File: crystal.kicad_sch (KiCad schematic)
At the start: 3 parts, among them X2 25000000

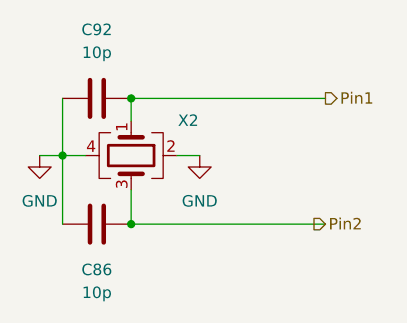
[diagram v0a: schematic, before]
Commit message: adds crystal for STM. Refs: #1
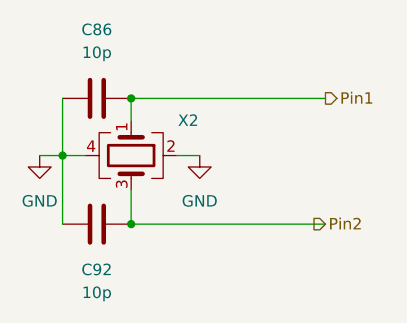
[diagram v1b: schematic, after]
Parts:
- renumbered C92 to C86, C86 to C92
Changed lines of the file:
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@@
 		(instances
 			(project "shish-lan"
-				(path "/d4536448-b109-4159-96e2-3dc21baf2d6e/06488c82-a47f-4277-b0ee-3bd211d8922a/2f245240-4d2b-41c8-b841-446fd2f2d0c3"
+				(path "/d4536448-b109-4159-96e2-3dc21baf2d6e/06488c82-a47f-4277-b0ee-3bd211d8922a/14851be8-da71-4848-89bd-314ca44f089b"
 					(reference "#PWR075")
 					(unit 1)
@@
 		(dnp no)
 		(fields_autoplaced yes)
-		(property "Reference" "C86"
+		(property "Reference" "C92"
 			(at 138.43 107.95 90)
 			(effects
@@
 		(instances
 			(project "shish-lan"
-				(path "/d4536448-b109-4159-96e2-3dc21baf2d6e/06488c82-a47f-4277-b0ee-3bd211d8922a/2f245240-4d2b-41c8-b841-446fd2f2d0c3"
-					(reference "C86")
+				(path "/d4536448-b109-4159-96e2-3dc21baf2d6e/06488c82-a47f-4277-b0ee-3bd211d8922a/14851be8-da71-4848-89bd-314ca44f089b"
+					(reference "C92")
 					(unit 1)
 				)
@@
 		(instances
 			(project "shish-lan"
-				(path "/d4536448-b109-4159-96e2-3dc21baf2d6e/06488c82-a47f-4277-b0ee-3bd211d8922a/2f245240-4d2b-41c8-b841-446fd2f2d0c3"
+				(path "/d4536448-b109-4159-96e2-3dc21baf2d6e/06488c82-a47f-4277-b0ee-3bd211d8922a/14851be8-da71-4848-89bd-314ca44f089b"
 					(reference "#PWR076")
 					(unit 1)
@@
 		(dnp no)
 		(fields_autoplaced yes)
-		(property "Reference" "C92"
+		(property "Reference" "C86"
 			(at 138.43 81.28 90)
 			(effects
@@
 		(instances
 			(project "shish-lan"
-				(path "/d4536448-b109-4159-96e2-3dc21baf2d6e/06488c82-a47f-4277-b0ee-3bd211d8922a/2f245240-4d2b-41c8-b841-446fd2f2d0c3"
-					(reference "C92")
+				(path "/d4536448-b109-4159-96e2-3dc21baf2d6e/06488c82-a47f-4277-b0ee-3bd211d8922a/14851be8-da71-4848-89bd-314ca44f089b"
+					(reference "C86")
 					(unit 1)
 				)
@@
 		(instances
 			(project "shish-lan"
-				(path "/d4536448-b109-4159-96e2-3dc21baf2d6e/06488c82-a47f-4277-b0ee-3bd211d8922a/2f245240-4d2b-41c8-b841-446fd2f2d0c3"
+				(path "/d4536448-b109-4159-96e2-3dc21baf2d6e/06488c82-a47f-4277-b0ee-3bd211d8922a/14851be8-da71-4848-89bd-314ca44f089b"
 					(reference "X2")
 					(unit 1)

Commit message: Uses crystal sheet in all places. Refs: #1
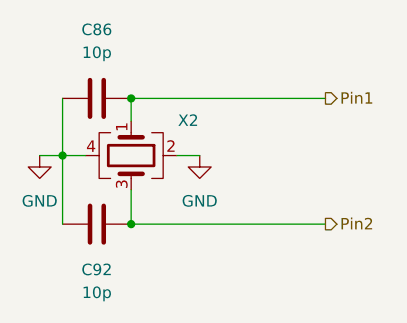
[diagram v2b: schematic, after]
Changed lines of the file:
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@@
 	(hierarchical_label "Pin2"
 		(shape output)
-		(at 162.56 102.87 0)
+		(at 163.83 102.87 0)
 		(effects
 			(font
@@
 					(unit 1)
 				)
+				(path "/d4536448-b109-4159-96e2-3dc21baf2d6e/0b7d9af9-83c1-43fa-a7a0-a33d0a00ea9c/d7edf10b-e7e7-437a-ab6c-966f29ad8f7f/48840ae5-c8f2-47ca-9691-b0413813be50"
+					(reference "#PWR075")
+					(unit 1)
+				)
 			)
 		)
@@
 					(unit 1)
 				)
+				(path "/d4536448-b109-4159-96e2-3dc21baf2d6e/0b7d9af9-83c1-43fa-a7a0-a33d0a00ea9c/d7edf10b-e7e7-437a-ab6c-966f29ad8f7f/48840ae5-c8f2-47ca-9691-b0413813be50"
+					(reference "C92")
+					(unit 1)
+				)
 			)
 		)
@@
 					(unit 1)
 				)
+				(path "/d4536448-b109-4159-96e2-3dc21baf2d6e/0b7d9af9-83c1-43fa-a7a0-a33d0a00ea9c/d7edf10b-e7e7-437a-ab6c-966f29ad8f7f/48840ae5-c8f2-47ca-9691-b0413813be50"
+					(reference "#PWR076")
+					(unit 1)
+				)
 			)
 		)
@@
 					(unit 1)
 				)
+				(path "/d4536448-b109-4159-96e2-3dc21baf2d6e/0b7d9af9-83c1-43fa-a7a0-a33d0a00ea9c/d7edf10b-e7e7-437a-ab6c-966f29ad8f7f/48840ae5-c8f2-47ca-9691-b0413813be50"
+					(reference "C86")
+					(unit 1)
+				)
 			)
 		)
@@
 					(reference "X2")
 					(unit 1)
+				)
+				(path "/d4536448-b109-4159-96e2-3dc21baf2d6e/0b7d9af9-83c1-43fa-a7a0-a33d0a00ea9c/d7edf10b-e7e7-437a-ab6c-966f29ad8f7f/48840ae5-c8f2-47ca-9691-b0413813be50"
+					(reference "X2")
+					(unit 1)

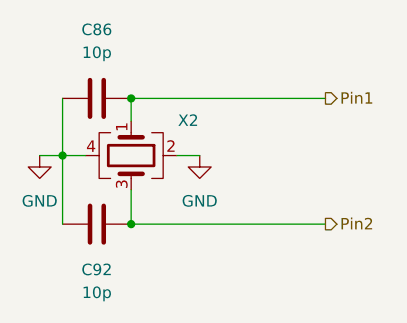
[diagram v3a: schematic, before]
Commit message: fixes ERC errors in DC/DC converters
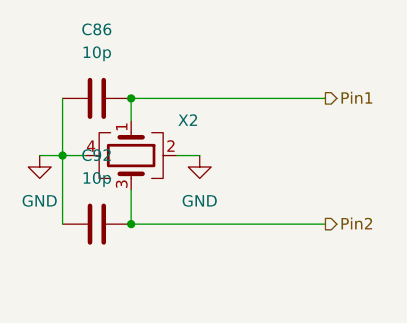
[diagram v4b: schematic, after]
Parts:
- C86, C92: footprint Capacitor_SMD:C_0201_0603Metric -> KL_Footprints:C_0603
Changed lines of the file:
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@@
 		(fields_autoplaced yes)
 		(property "Reference" "C92"
-			(at 138.43 107.95 90)
+			(at 138.43 95.25 90)
 			(effects
 				(font
@@
 		)
 		(property "Value" "10p"
-			(at 138.43 110.49 90)
-			(effects
-				(font
-					(size 1.27 1.27)
-				)
-			)
-		)
-		(property "Footprint" "Capacitor_SMD:C_0201_0603Metric"
+			(at 138.43 97.79 90)
+			(effects
+				(font
+					(size 1.27 1.27)
+				)
+			)
+		)
+		(property "Footprint" "KL_Footprints:C_0603"
 			(at 134.62 103.8352 0)
 			(effects
@@
 			)
 		)
-		(property "Footprint" "Capacitor_SMD:C_0201_0603Metric"
+		(property "Footprint" "KL_Footprints:C_0603"
 			(at 134.62 89.8652 0)
 			(effects

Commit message: removes unused busses, adds cheaper 0R resistor, clean up to fix ERC errors. Refs: #1
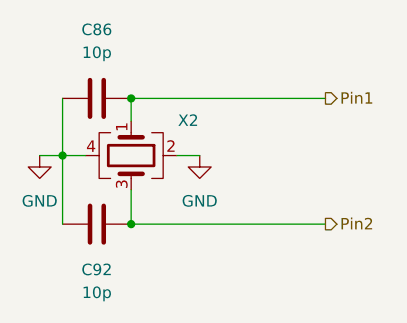
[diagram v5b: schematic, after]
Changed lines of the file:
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@@
 		(fields_autoplaced yes)
 		(property "Reference" "C92"
-			(at 138.43 95.25 90)
+			(at 138.43 107.95 90)
 			(effects
 				(font
@@
 		)
 		(property "Value" "10p"
-			(at 138.43 97.79 90)
+			(at 138.43 110.49 90)
 			(effects
 				(font
